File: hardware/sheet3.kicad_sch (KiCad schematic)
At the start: 0 parts

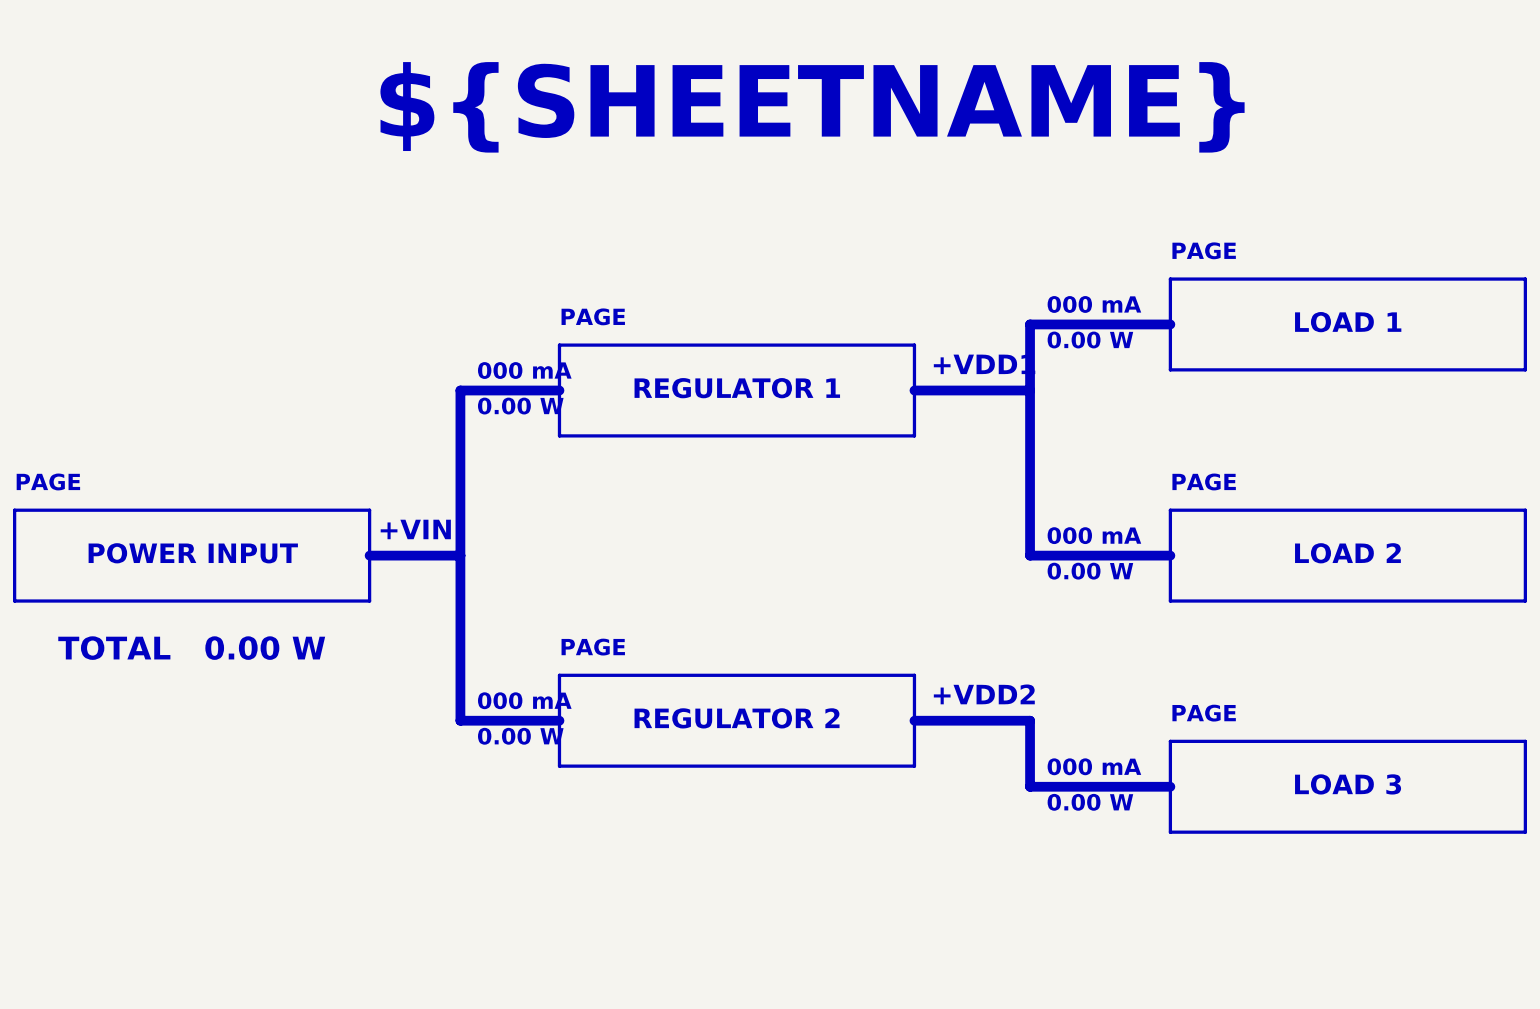
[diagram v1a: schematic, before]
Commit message: hardware(feat): change power budget to power supply
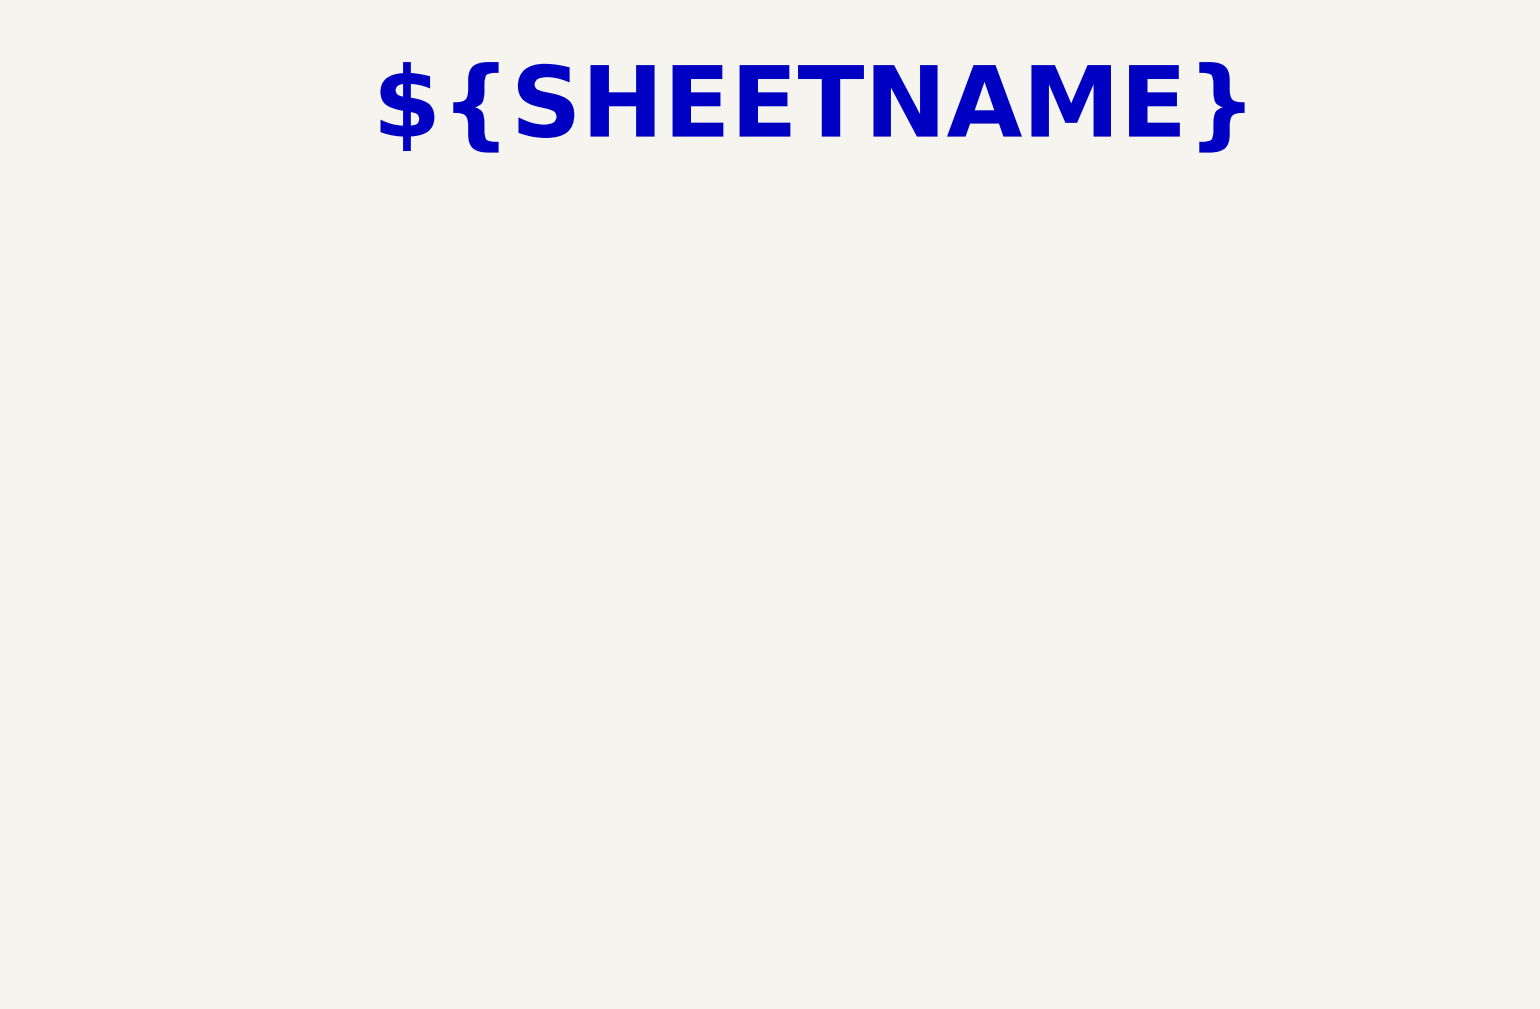
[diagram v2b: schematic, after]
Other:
- note removed: "+VDD1"
- note removed: "+VDD2"
- note removed: "+VIN"
- note removed: "0.00 W"
- note removed: "000 mA"
- note removed: "LOAD 1"
- note removed: "LOAD 2"
- note removed: "LOAD 3"
- note removed: "PAGE"
- note removed: "POWER INPUT"
- note removed: "REGULATOR 1"
- note removed: "REGULATOR 2"
- note removed: "TOTAL 0.00 W"

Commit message: hardware(feat): add buck regulator
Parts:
- added C1: 47uF, 02_capacitors:CP_Elec_6.3x5.8, symbol 02_capacitors:CAP-E_47uF-50V-20%-D6.3x5.8
- added C2: 10uF, 02_capacitors:C_1210_3225Metric, symbol 02_capacitors:CAP_10uF-50V-10%-X7R-1210
- added C3, C4, C7: 100nF, 02_capacitors:C_0603_1608Metric, symbol 02_capacitors:CAP_100nF-50V-10%-X7R-0603
- added C5, C6: 22uF, 02_capacitors:C_1210_3225Metric, symbol 02_capacitors:CAP_22uF-25V-10%-X7R-1210
- added D1: B340AE-13, 04_diodes:D_SMA, symbol 04_diodes:DIO-S_40V-3A-0.5V-DO-214AC
- added D2: SMAJ33A, 04_diodes:D_SMA, symbol 04_diodes:DIO-T_33V-53.3V-DO-214AC
- added J1: DC-005-5A-2.0, 08_connectors:TH_DC-005-5A-2.0, symbol 08_connectors:CON-PWR_DC-005-5A-2.0
- added L1: 4.7uH, 03_inductors:L_1008_2520Metric, symbol 03_inductors:IND_4.7uH-1.5A-20%-1008
- added U1: AP63205WU-7, 06_ics:TSOT-23-6, symbol 06_ics:IC-DCDC_AP63205WU-7
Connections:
- new net: C4.2, L1.1, U1.5 (SW)
- new net: C4.1, U1.6 (BST)
- new net: D1.2 (A), J1.1
- new net +12V: C1.1, C2.1, C3.1, D1.1 (K), D2.1 (K), U1.2 (EN), U1.3 (VIN)
- new net +5V: C5.1, C6.1, C7.1, L1.2, U1.1 (FB)
- new net GND: C1.2, C2.2, C3.2, C5.2, C6.2, C7.2, D2.2 (A), J1.2, J1.3, U1.4 (GND)
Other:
- note added: "BUCK REGULATOR (+5V)"
- note added: "Input Protections"

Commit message: hardware(feat): add mcu
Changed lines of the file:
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@@
+					(unit 1)
+				)
+				(path "/08767502-fa14-4976-aaca-9650785a2144/90f70198-c0ab-4cef-90bd-cd1364d30a2f"
+					(reference "C9")
 					(unit 1)
 				)
@@
 					(unit 1)
 				)
+				(path "/08767502-fa14-4976-aaca-9650785a2144/90f70198-c0ab-4cef-90bd-cd1364d30a2f"
+					(reference "#PWR011")
+					(unit 1)
+				)
 			)
 		)
@@
 		(on_board yes)
 		(dnp no)
-		(fields_autoplaced yes)
 		(property "Reference" "#PWR05"
 			(at 228.6 92.71 0)
@@
 		)
 		(property "Value" "GND"
-			(at 228.6 91.44 0)
+			(at 228.6 90.17 0)
 			(effects
 				(font
@@
 					(unit 1)
 				)
+				(path "/08767502-fa14-4976-aaca-9650785a2144/90f70198-c0ab-4cef-90bd-cd1364d30a2f"
+					(reference "U2")
+					(unit 1)
+				)
 			)
 		)
@@
 					(unit 1)
 				)
+				(path "/08767502-fa14-4976-aaca-9650785a2144/90f70198-c0ab-4cef-90bd-cd1364d30a2f"
+					(reference "D3")
+					(unit 1)
+				)
 			)
 		)
@@
 					(unit 1)
 				)
+				(path "/08767502-fa14-4976-aaca-9650785a2144/90f70198-c0ab-4cef-90bd-cd1364d30a2f"
+					(reference "#PWR07")
+					(unit 1)
+				)
 			)
 		)
@@
 					(unit 1)
 				)
+				(path "/08767502-fa14-4976-aaca-9650785a2144/90f70198-c0ab-4cef-90bd-cd1364d30a2f"
+					(reference "D4")
+					(unit 1)
+				)
 			)
 		)
@@
 					(unit 1)
 				)
+				(path "/08767502-fa14-4976-aaca-9650785a2144/90f70198-c0ab-4cef-90bd-cd1364d30a2f"
+					(reference "L2")
+					(unit 1)
+				)
 			)
 		)
@@
 				(path "/08767502-fa14-4976-aaca-9650785a2144/15087690-13d4-4a2e-883d-52edd77e88dd"
 					(reference "C3")
+					(unit 1)
+				)
+				(path "/08767502-fa14-4976-aaca-9650785a2144/90f70198-c0ab-4cef-90bd-cd1364d30a2f"
+					(reference "C10")
 					(unit 1)
 				)
@@
 					(unit 1)
 				)
+				(path "/08767502-fa14-4976-aaca-9650785a2144/90f70198-c0ab-4cef-90bd-cd1364d30a2f"
+					(reference "#FLG05")
+					(unit 1)
+				)
 			)
 		)
@@
 				(path "/08767502-fa14-4976-aaca-9650785a2144/15087690-13d4-4a2e-883d-52edd77e88dd"
 					(reference "C1")
+					(unit 1)
+				)
+				(path "/08767502-fa14-4976-aaca-9650785a2144/90f70198-c0ab-4cef-90bd-cd1364d30a2f"
+					(reference "C8")
 					(unit 1)
 				)
@@
 					(unit 1)
 				)
+				(path "/08767502-fa14-4976-aaca-9650785a2144/90f70198-c0ab-4cef-90bd-cd1364d30a2f"
+					(reference "J2")
+					(unit 1)
+				)
 			)
 		)
@@
 					(unit 1)
 				)
+				(path "/08767502-fa14-4976-aaca-9650785a2144/90f70198-c0ab-4cef-90bd-cd1364d30a2f"
+					(reference "C12")
+					(unit 1)
+				)

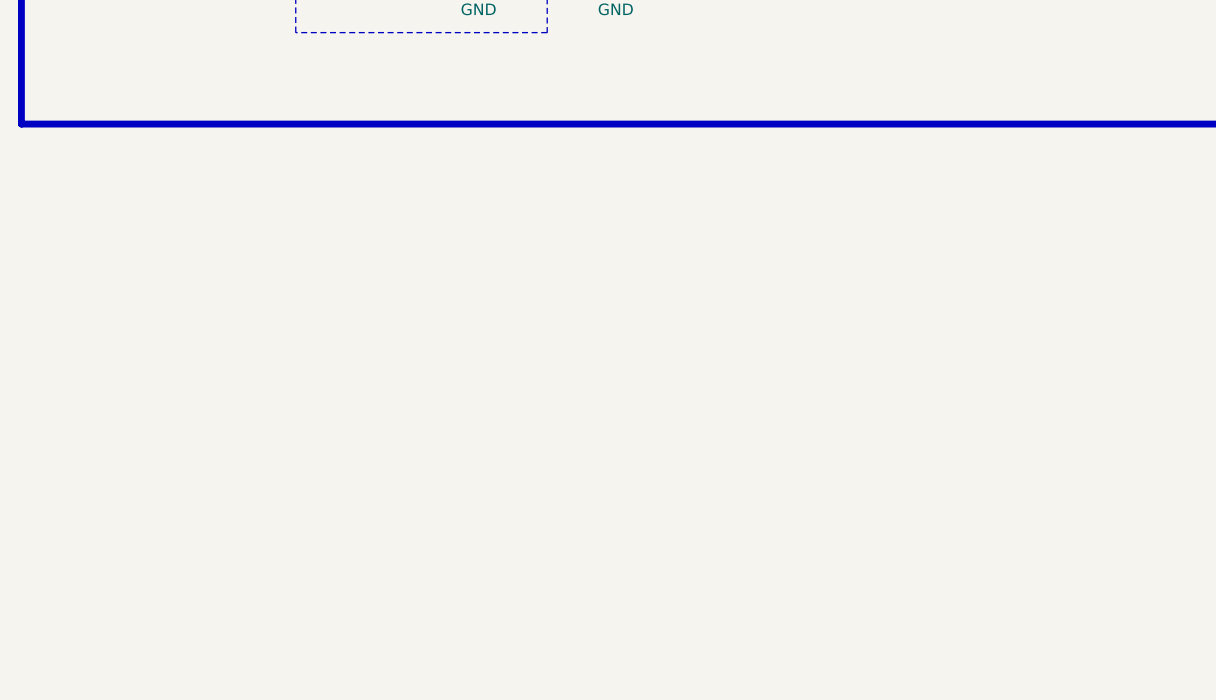
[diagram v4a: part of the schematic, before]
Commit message: hardware(feat): add ldo regulator to +3V3
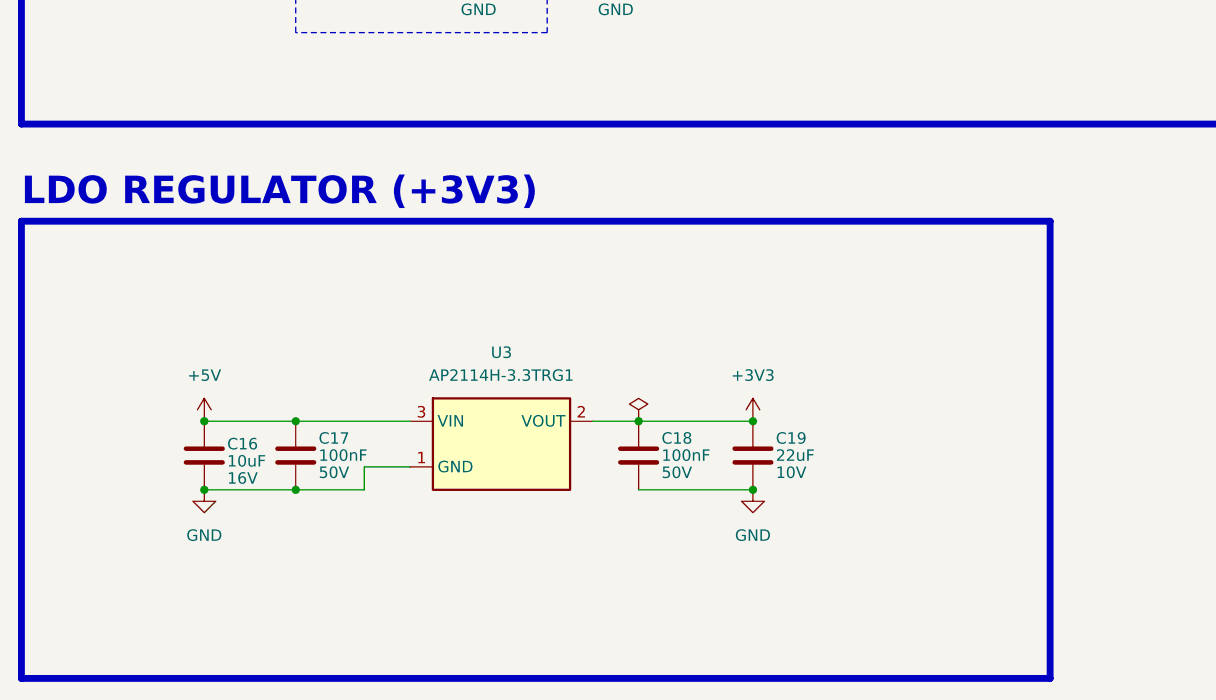
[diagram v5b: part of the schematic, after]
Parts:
- added C16: 10uF, 02_capacitors:C_0805_2012Metric, symbol 02_capacitors:CAP_10uF-16V-10%-X5R-0805
- added C17, C18: 100nF, 02_capacitors:C_0603_1608Metric, symbol 02_capacitors:CAP_100nF-50V-10%-X7R-0603
- added C19: 22uF, 02_capacitors:C_0805_2012Metric, symbol 02_capacitors:CAP_22uF-10V-20%-X5R-0805
- added U3: AP2114H-3.3TRG1, 06_ics:SOT-223-3_TabPin2, symbol 06_ics:IC-LDO_AP2114H-3.3TRG1
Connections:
- net +5V: now also C16.1, C17.1, U3.3 (VIN)
- net GND: now also C16.2, C17.2, C18.2, C19.2, U3.1 (GND)
- new net +3V3: C18.1, C19.1, U3.2 (VOUT)
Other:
- note added: "LDO REGULATOR (+3V3)"

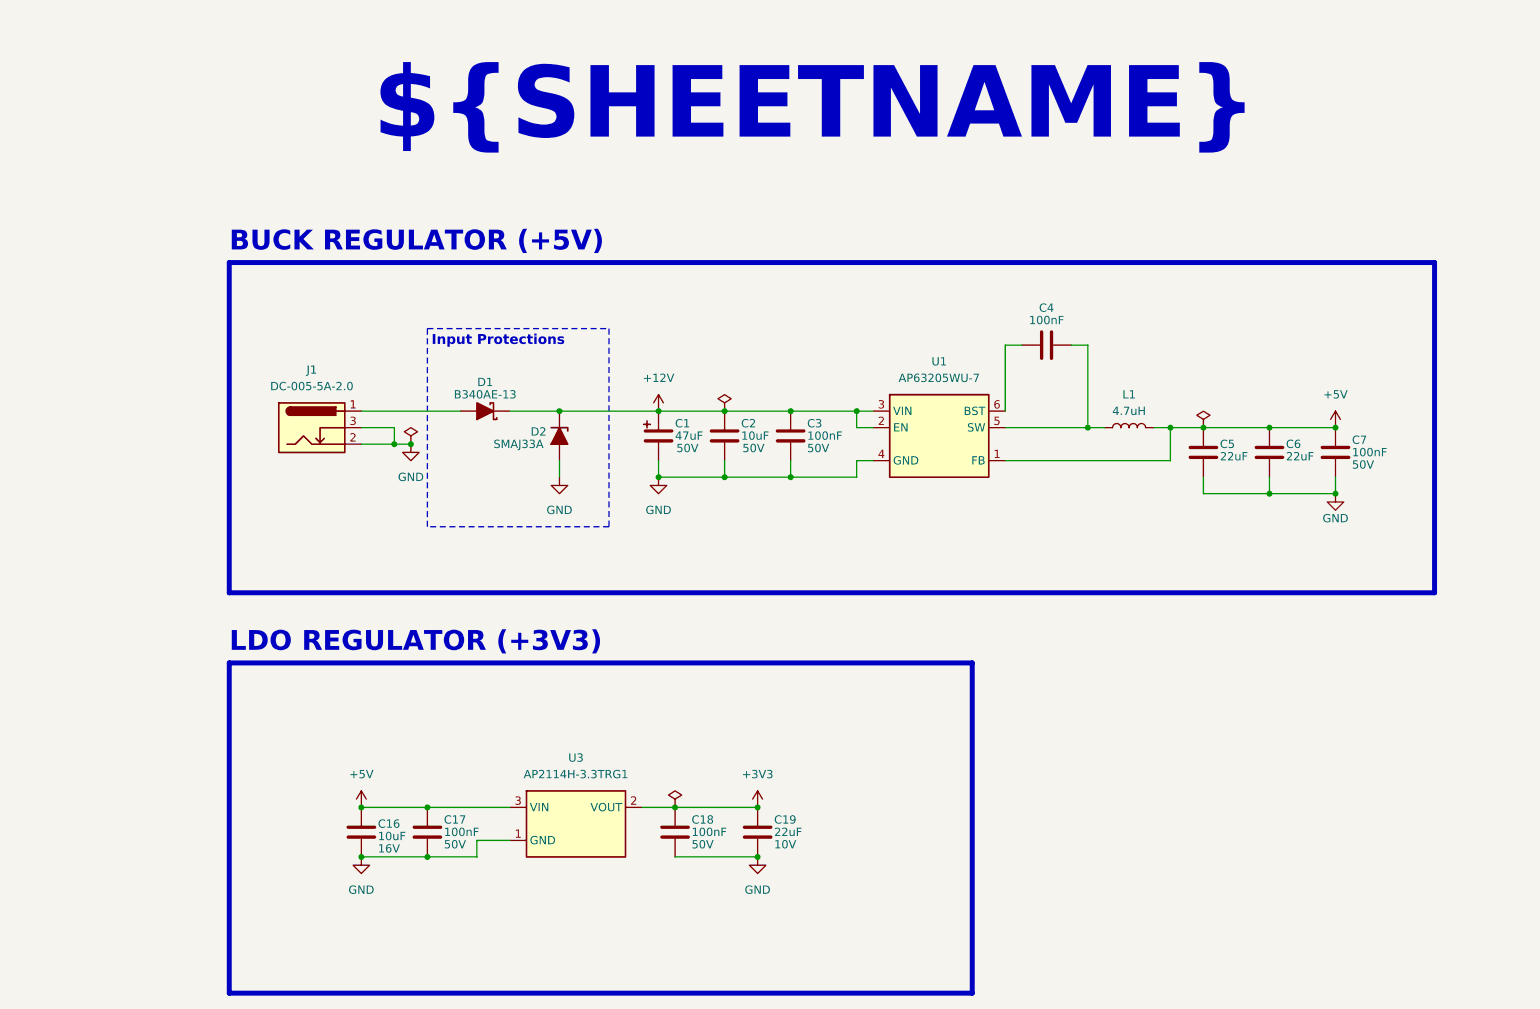
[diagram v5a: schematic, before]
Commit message: hardware(feat): add led indications
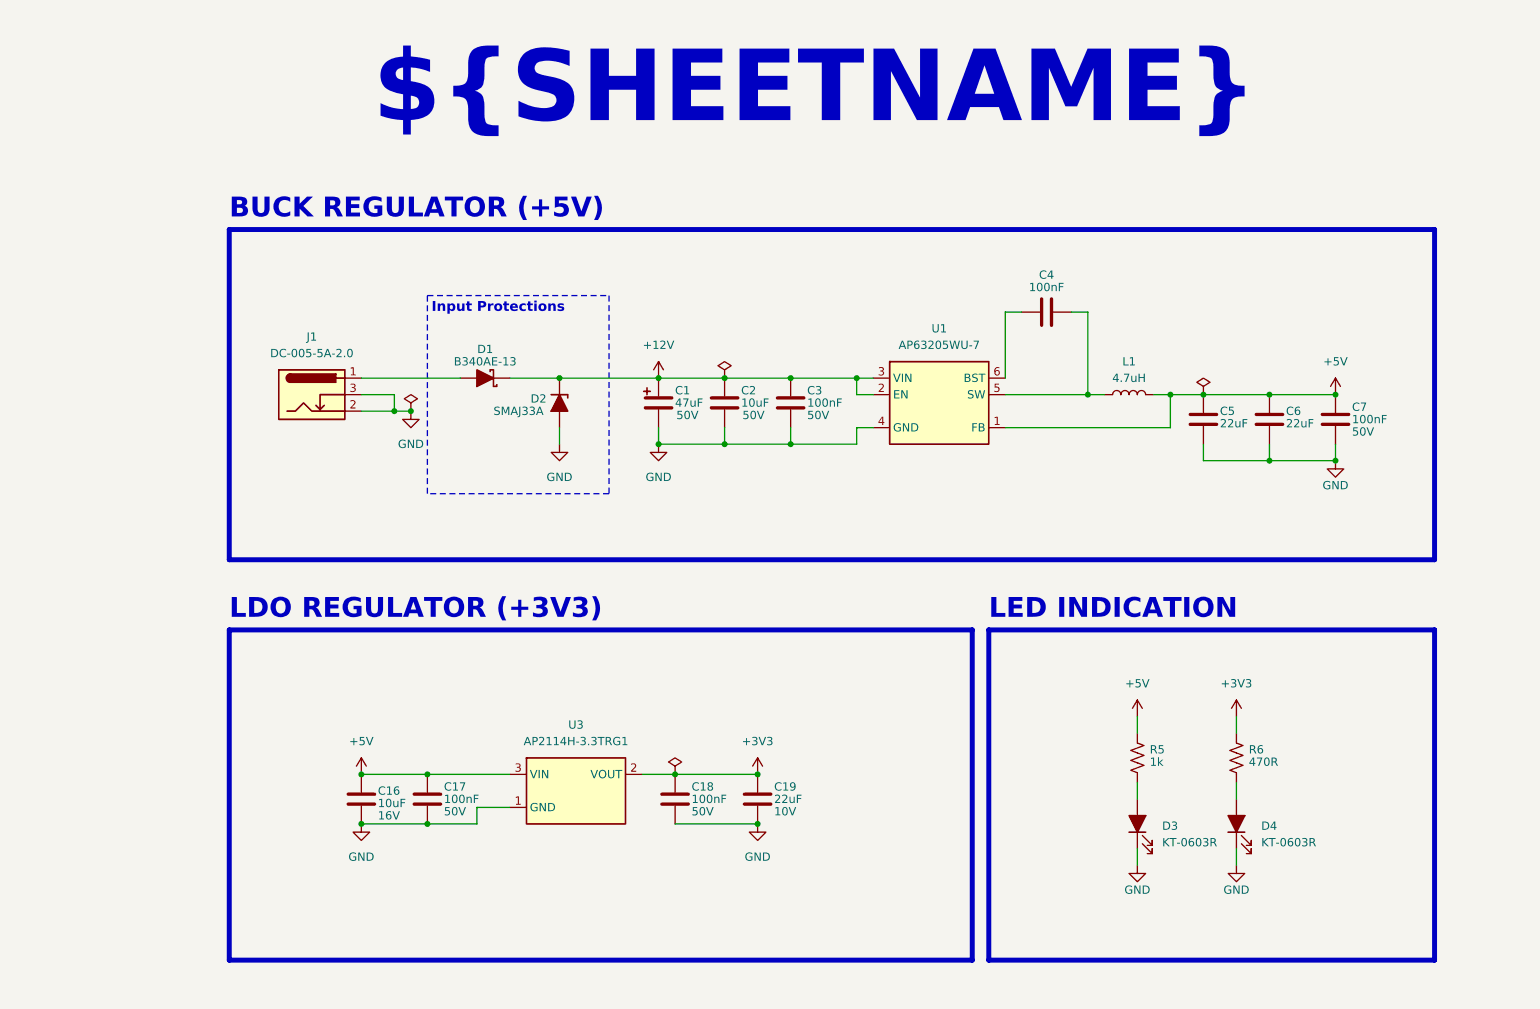
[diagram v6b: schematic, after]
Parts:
- added D3, D4: KT-0603R, 04_diodes:LED_0603_1608Metric, symbol 04_diodes:LED_RED-2V-20mA-0603
- added R5: 1k, 01_resistors:R_0603_1608Metric, symbol 01_resistors:RES_1K-0.1W-1%-0603
- added R6: 470R, 01_resistors:R_0603_1608Metric, symbol 01_resistors:RES_470R-0.1W-1%-0603
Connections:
- net +3V3: now also R6.1
- net +5V: now also R5.1
- net GND: now also D3.1 (K), D4.1 (K)
- new net: D3.2 (A), R5.2
- new net: D4.2 (A), R6.2
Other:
- note added: "LED INDICATION"
- moved on the sheet: C1, C16, C17, C18, C19, C2, C3, C4, C5, C6, C7, D1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

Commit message: hardware(feat): add usb connector with esd (#1)
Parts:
- added R10: 100k, 01_resistors:R_0603_1608Metric, symbol 01_resistors:RES_100K-0.1W-1%-0603
- added R11: 22k, 01_resistors:R_0603_1608Metric, symbol 01_resistors:RES_22K-0.1W-1%-0603
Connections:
- net +12V: now also R10.1; no longer U1.2 (EN)
- net GND: now also R11.2
- new net: R10.2, R11.1, U1.2 (EN)
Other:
- moved on the sheet: C4, C5, C6, C7, L1, U1
